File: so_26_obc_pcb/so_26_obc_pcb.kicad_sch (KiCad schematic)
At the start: 41 parts, among them J1 Conn_02x12_Odd_Even, J2 Conn_02x06_Odd_Even, J3 Conn_01x04, J4 Conn_01x03, J5 Conn_01x03, SW1 SW_Push, U1 STM32G431RBTx, U2 MPRLS0025, U3 PCT2075, U4 LSM6DS3, U5 MEM2067-02-180-00-A

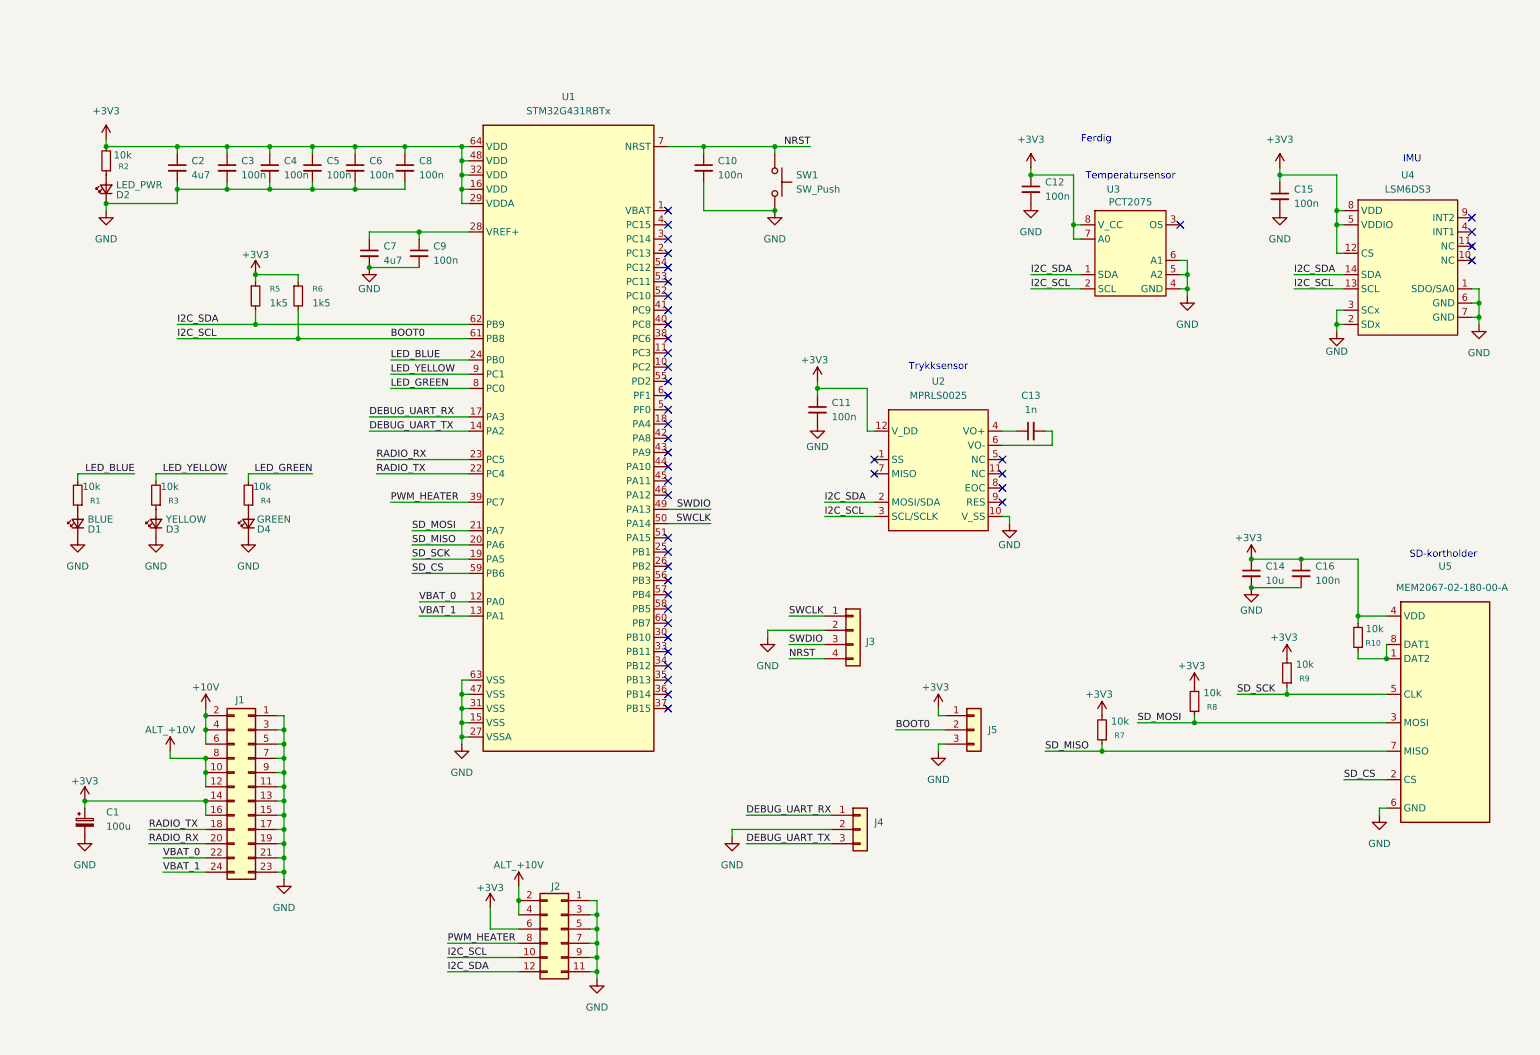
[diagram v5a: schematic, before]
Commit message: Schematic: Added symbol for level shifter, updated footprint for pressure sensor
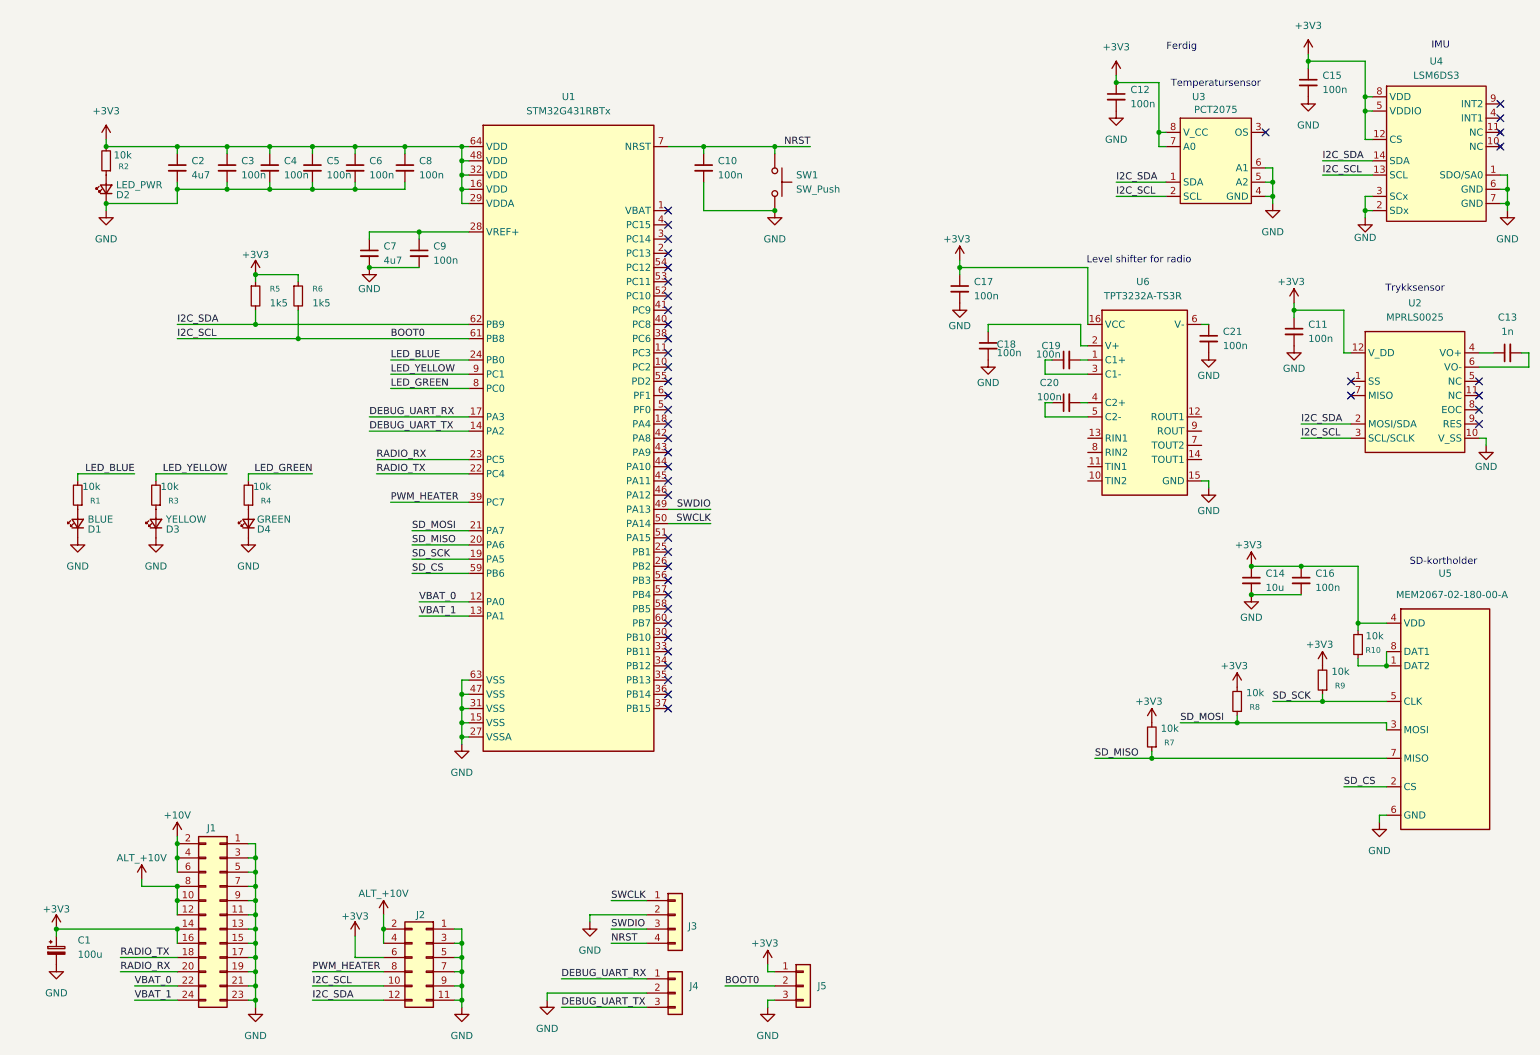
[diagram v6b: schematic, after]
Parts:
- added C17, C18, C19, C20, C21: 100n, Capacitor_SMD:C_0805_2012Metric_Pad1.18x1.45mm_HandSolder, symbol Device:C_Small
- added U6: TPT3232A-TS3R, symbol so_26_obc_library:TPT3232A-TS3R
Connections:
- net +3V3: now also C17.1, U6.16 (VCC)
- net GND: now also C17.2, C18.2, C21.2, U6.15 (GND)
- new net: C21.1, U6.6 (V-)
- new net: C19.2, U6.1 (C1+)
- new net: C18.1, U6.2 (V+)
- new net: C19.1, U6.3 (C1-)
- new net: C20.2, U6.4 (C2+)
- new net: C20.1, U6.5 (C2-)
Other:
- note added: "Level shifter for radio"
- moved on the sheet: C1, C11, C12, C13, C14, C15, C16, J1, J2, J3, J4, J5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

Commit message: Schematic: added low_power_mode
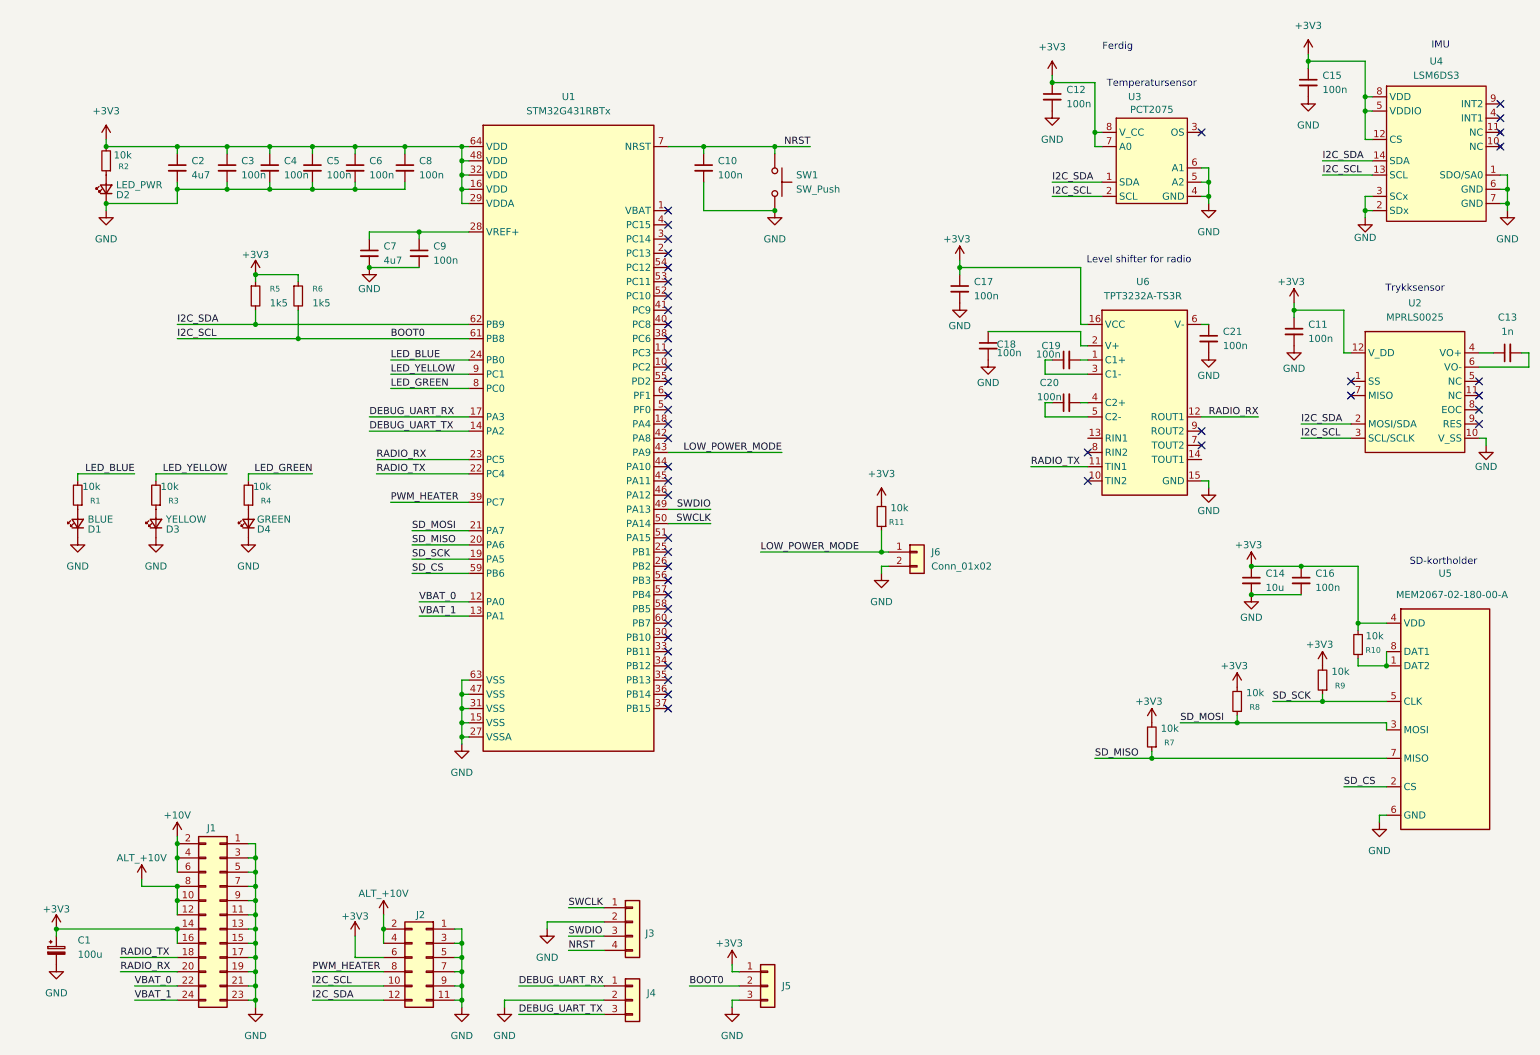
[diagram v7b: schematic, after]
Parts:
- added J6: Conn_01x02, Connector_PinSocket_2.54mm:PinSocket_1x02_P2.54mm_Vertical, symbol Connector_Generic:Conn_01x02
- added R11: 10k, Resistor_SMD:R_0805_2012Metric_Pad1.20x1.40mm_HandSolder, symbol Device:R_Small
- U6: footprint (none) -> Package_SO:TSSOP-16_4.4x5mm_P0.65mm
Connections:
- net +3V3: now also R11.2
- net GND: now also J6.2 (Pin_2)
- net RADIO_RX: now also U6.12 (ROUT1)
- net RADIO_TX: now also U6.11 (TIN1)
- net LOW_POWER_MODE: now reaches U1.43 (PA9)
- net LOW_POWER_MODE: now also J6.1 (Pin_1), R11.1
- no-connect marks 45 -> 48
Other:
- moved on the sheet: C12, J3, J4, J5, U3

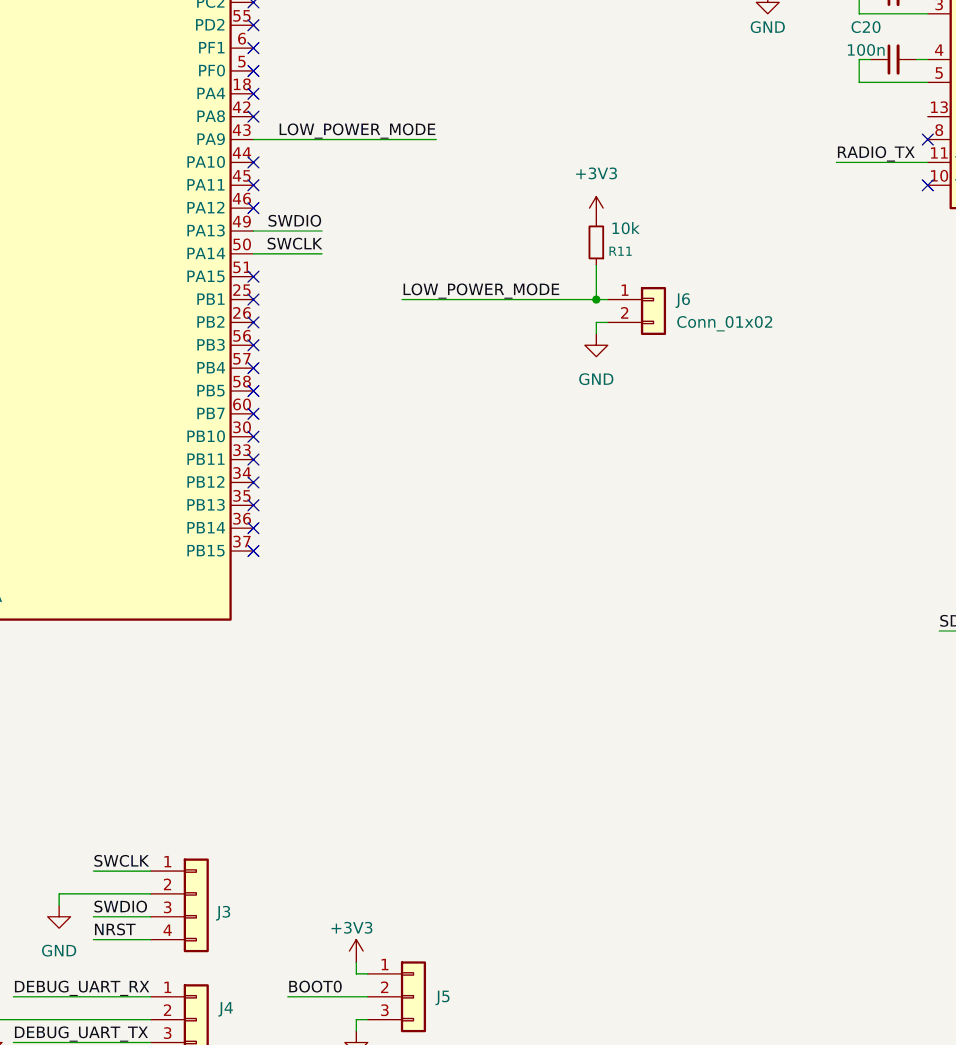
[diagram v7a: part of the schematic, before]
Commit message: PCB: changed settings to match specs from JCL
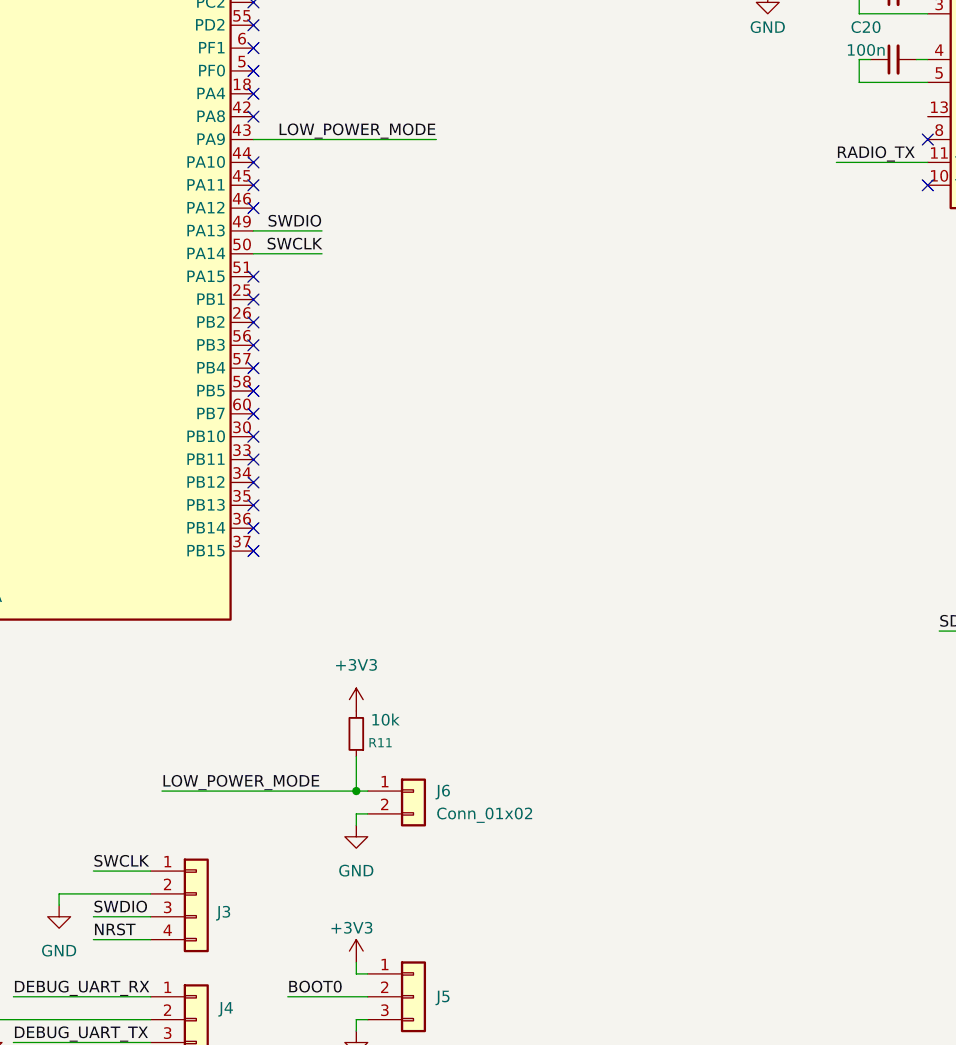
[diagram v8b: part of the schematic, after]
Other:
- moved on the sheet: J6, R11
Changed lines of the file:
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@@
 	)
 	(junction
-		(at 166.37 110.49)
+		(at 139.7 165.1)
 		(diameter 0)
 		(color 0 0 0 0)
@@
 	(wire
 		(pts
-			(xy 166.37 113.03) (xy 167.64 113.03)
+			(xy 139.7 167.64) (xy 140.97 167.64)
 		)
 		(stroke
@@
 	(wire
 		(pts
-			(xy 166.37 110.49) (xy 167.64 110.49)
+			(xy 139.7 165.1) (xy 140.97 165.1)
 		)
 		(stroke
@@
 	(wire
 		(pts
-			(xy 144.78 110.49) (xy 166.37 110.49)
+			(xy 118.11 165.1) (xy 139.7 165.1)
 		)
 		(stroke
@@
 	(wire
 		(pts
-			(xy 166.37 114.3) (xy 166.37 113.03)
+			(xy 139.7 168.91) (xy 139.7 167.64)
 		)
 		(stroke
@@
 	(wire
 		(pts
-			(xy 166.37 106.68) (xy 166.37 110.49)
+			(xy 139.7 161.29) (xy 139.7 165.1)
 		)
 		(stroke
@@
 	)
 	(label "LOW_POWER_MODE"
-		(at 144.78 110.49 0)
+		(at 118.11 165.1 0)
 		(effects
 			(font
@@
 	(symbol
 		(lib_id "Device:R_Small")
-		(at 166.37 104.14 180)
+		(at 139.7 158.75 180)
 		(unit 1)
 		(exclude_from_sim no)
@@
 		(dnp no)
 		(property "Reference" "R11"
-			(at 170.434 105.156 0)
+			(at 143.764 159.766 0)
 			(effects
 				(font
@@
 		)
 		(property "Value" "10k"
-			(at 171.196 102.616 0)
+			(at 144.526 157.226 0)
 			(effects
 				(font
@@
 		)
 		(property "Footprint" "Resistor_SMD:R_0805_2012Metric_Pad1.20x1.40mm_HandSolder"
-			(at 166.37 104.14 0)
+			(at 139.7 158.75 0)
 			(effects
 				(font
@@
 		)
 		(property "Datasheet" "~"
-			(at 166.37 104.14 0)
+			(at 139.7 158.75 0)
 			(effects
 				(font
@@
 		)
 		(property "Description" "Resistor, small symbol"
-			(at 166.37 104.14 0)
+			(at 139.7 158.75 0)
 			(effects
 				(font
@@
 	(symbol
 		(lib_id "power:GND")
-		(at 166.37 114.3 0)
+		(at 139.7 168.91 0)
 		(unit 1)
 		(exclude_from_sim no)
@@
 		(fields_autoplaced yes)
 		(property "Reference" "#PWR043"
-			(at 166.37 120.65 0)
+			(at 139.7 175.26 0)
 			(effects
 				(font
@@
 		)
 		(property "Value" "GND"
-			(at 166.37 119.38 0)
+			(at 139.7 173.99 0)
 			(effects
 				(font
@@
 		)
 		(property "Footprint" ""
-			(at 166.37 114.3 0)
+			(at 139.7 168.91 0)
 			(effects
 				(font
@@
 		)
 		(property "Datasheet" ""
-			(at 166.37 114.3 0)
+			(at 139.7 168.91 0)
 			(effects
 				(font
@@
 		)
 		(property "Description" "Power symbol creates a global label with name \"GND\" , ground"
-			(at 166.37 114.3 0)
+			(at 139.7 168.91 0)
 			(effects
 				(font
@@
 	(symbol
 		(lib_id "Connector_Generic:Conn_01x02")
-		(at 172.72 110.49 0)
+		(at 146.05 165.1 0)
 		(unit 1)
 		(exclude_from_sim no)
@@
 		(fields_autoplaced yes)
 		(property "Reference" "J6"
-			(at 175.26 110.4899 0)
+			(at 148.59 165.0999 0)
 			(effects
 				(font
@@
 		)
 		(property "Value" "Conn_01x02"
-			(at 175.26 113.0299 0)
+			(at 148.59 167.6399 0)
 			(effects
 				(font
@@
 		)
 		(property "Footprint" "Connector_PinSocket_2.54mm:PinSocket_1x02_P2.54mm_Vertical"
-			(at 172.72 110.49 0)
+			(at 146.05 165.1 0)
 			(effects
 				(font
@@
 		)
 		(property "Datasheet" "~"
-			(at 172.72 110.49 0)
+			(at 146.05 165.1 0)
 			(effects
 				(font
@@
 		)
 		(property "Description" "Generic connector, single row, 01x02, script generated (kicad-library-utils/schlib/autogen/connector/)"
-			(at 172.72 110.49 0)
+			(at 146.05 165.1 0)
 			(effects
 				(font
@@
 	(symbol
 		(lib_id "power:+3V3")
-		(at 166.37 101.6 0)
+		(at 139.7 156.21 0)
 		(unit 1)
 		(exclude_from_sim no)
@@
 		(dnp no)
 		(property "Reference" "#PWR044"
-			(at 166.37 105.41 0)
+			(at 139.7 160.02 0)
 			(effects
 				(font
@@
 		)
 		(property "Value" "+3V3"
-			(at 166.37 96.52 0)
+			(at 139.7 151.13 0)
 			(effects
 				(font
@@
 		)
 		(property "Footprint" ""
-			(at 166.37 101.6 0)
+			(at 139.7 156.21 0)
 			(effects
 				(font
@@
 		)
 		(property "Datasheet" ""
-			(at 166.37 101.6 0)
+			(at 139.7 156.21 0)
 			(effects
 				(font
@@
 		)
 		(property "Description" "Power symbol creates a global label with name \"+3V3\""
-			(at 166.37 101.6 0)
+			(at 139.7 156.21 0)
 			(effects
 				(font
